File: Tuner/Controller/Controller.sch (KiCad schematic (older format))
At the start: 94 parts, among them J1 Conn_02x05_Odd_Even, J10 Conn_01x05, J12 Conn_01x02, J15 Conn_01x02, J16 Conn_01x06, J18 Conn_01x01, J19 Conn_01x01, J2 Conn_02x05_Odd_Even, J20 Conn_01x01, J21 Conn_01x01, J26 Conn_01x02, J27 Conn_01x02, J28 Conn_01x02, J3 Conn_02x05_Odd_Even, J30 Conn_01x02, J4 Conn_02x05_Odd_Even, J5 Conn_02x05_Odd_Even, J6 Conn_01x02, J7 Conn_01x02, J8 Conn_01x06, Q2 2N3904, U4 LM350_TO220

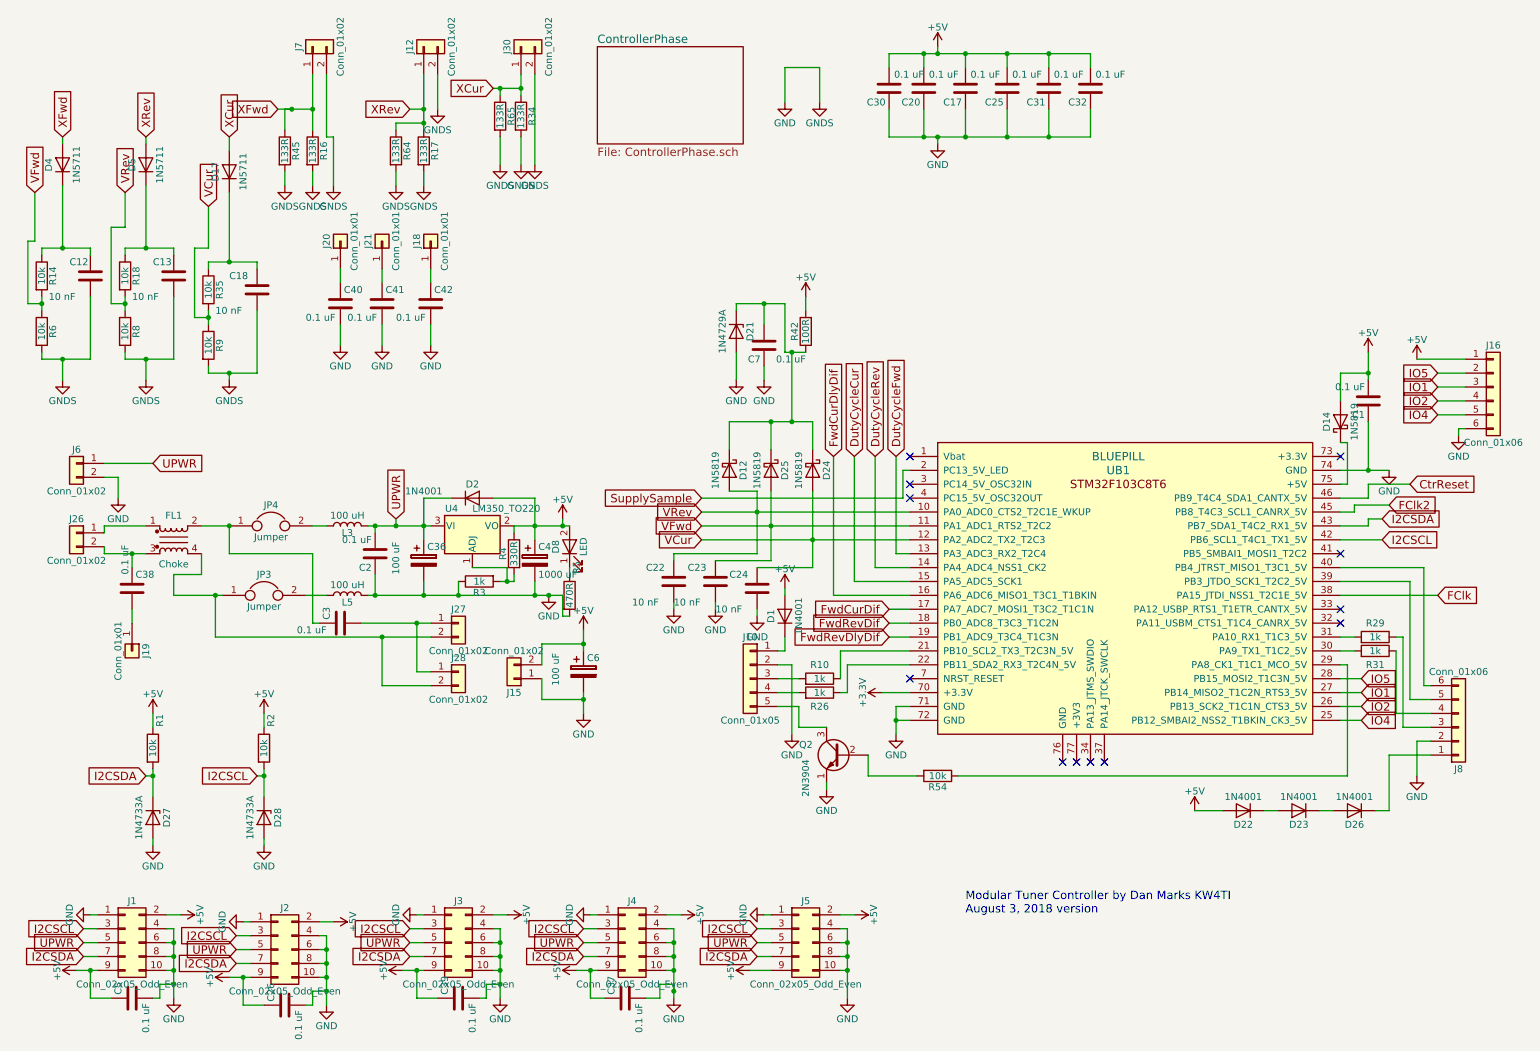
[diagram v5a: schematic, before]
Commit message: Added BNC and screw terminal combo pads
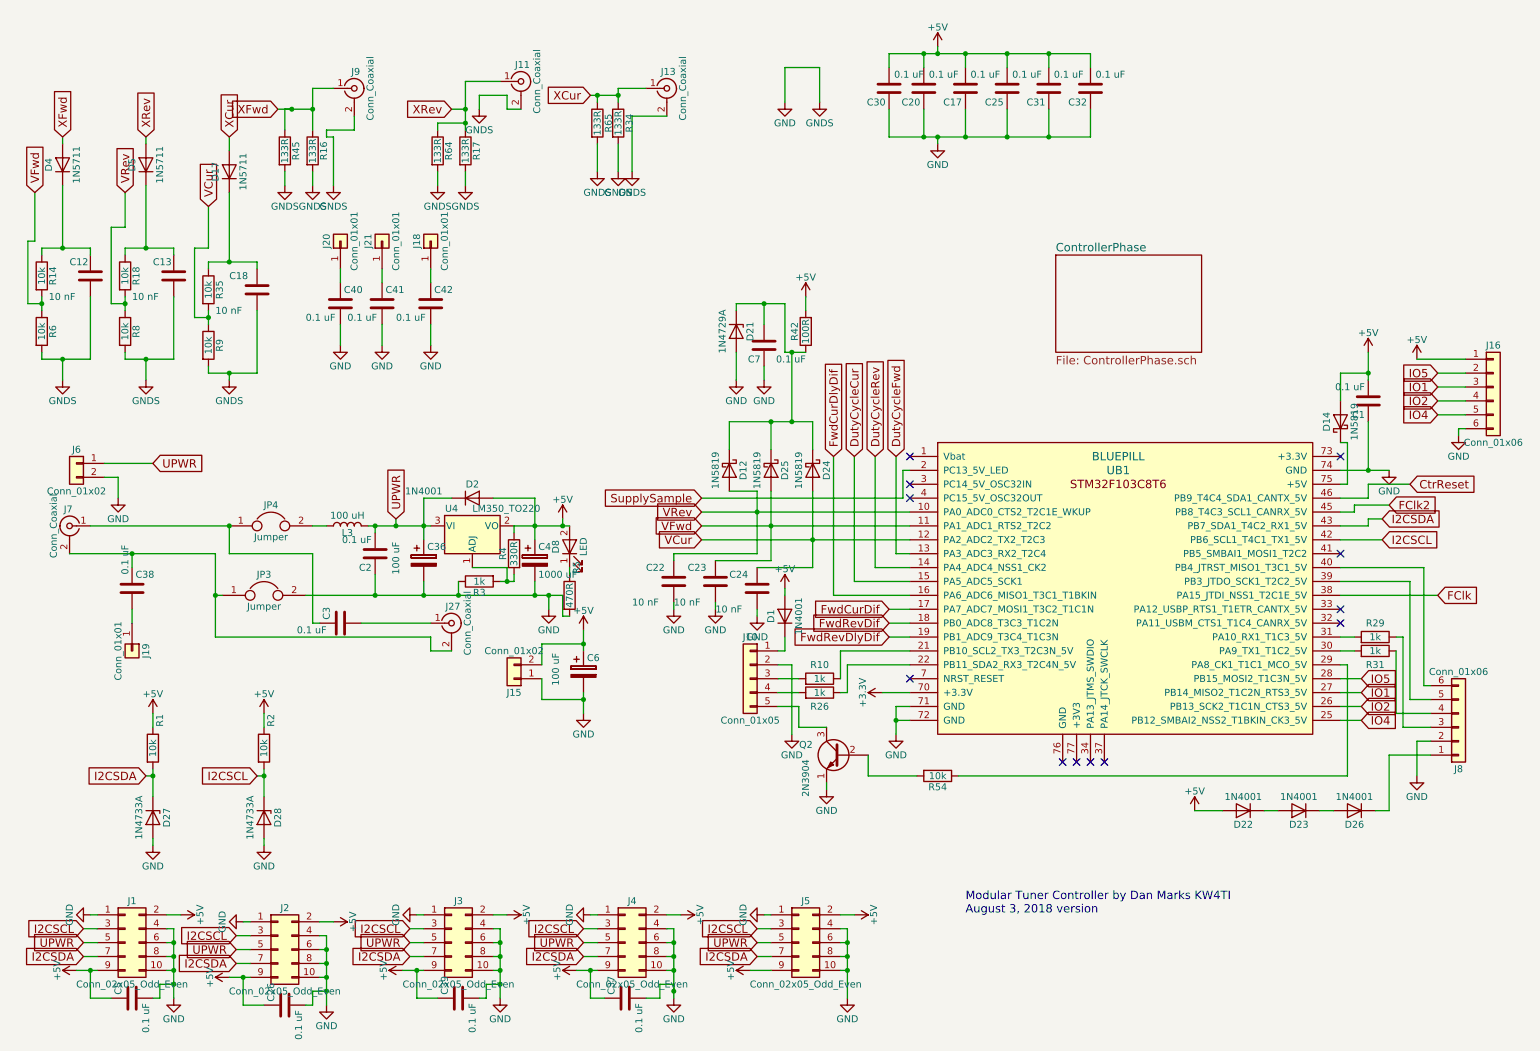
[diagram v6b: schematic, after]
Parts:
- removed FL1: Choke, Controller:GenericCMCL, symbol EMI_Filter_CommonMode
- removed J12, J26, J27, J28, J30, J7: Conn_01x02, Connectors_Terminal_Blocks:TerminalBlock_bornier-2_P5.08mm, symbol Conn_01x02
- removed L5: 100 uH, Inductors_THT:L_Toroid_Vertical_L14.0mm_W6.3mm_P4.57mm_Pulse_A, symbol L
- added J11, J13, J27, J7, J9: Conn_Coaxial, Controller:bnc_90_1-1337543-0_pad_combo, symbol Conn_Coaxial
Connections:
- net GND: now also JP3.2, J11.2 (Ext), J13.2 (Ext), J9.2 (Ext)
- net XCur: now also J13.1 (In)
- net XFwd: now also J9.1 (In)
- net XRev: now also J11.1 (In)
- net at C38.1: now also JP3.1, J27.2 (Ext), J7.2 (Ext)
- net at C3.2: now also J27.1 (In)
- net at C3.1, JP4.1: now also J7.1 (In)
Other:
- moved on the sheet: R17, R34, R64, R65

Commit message: A few tweaks
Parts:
- removed D22, D23, D26: 1N4001, Diodes_THT:D_DO-41_SOD81_P7.62mm_Horizontal, symbol D
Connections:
- net +5V: now also J8.1 (Pin_1)

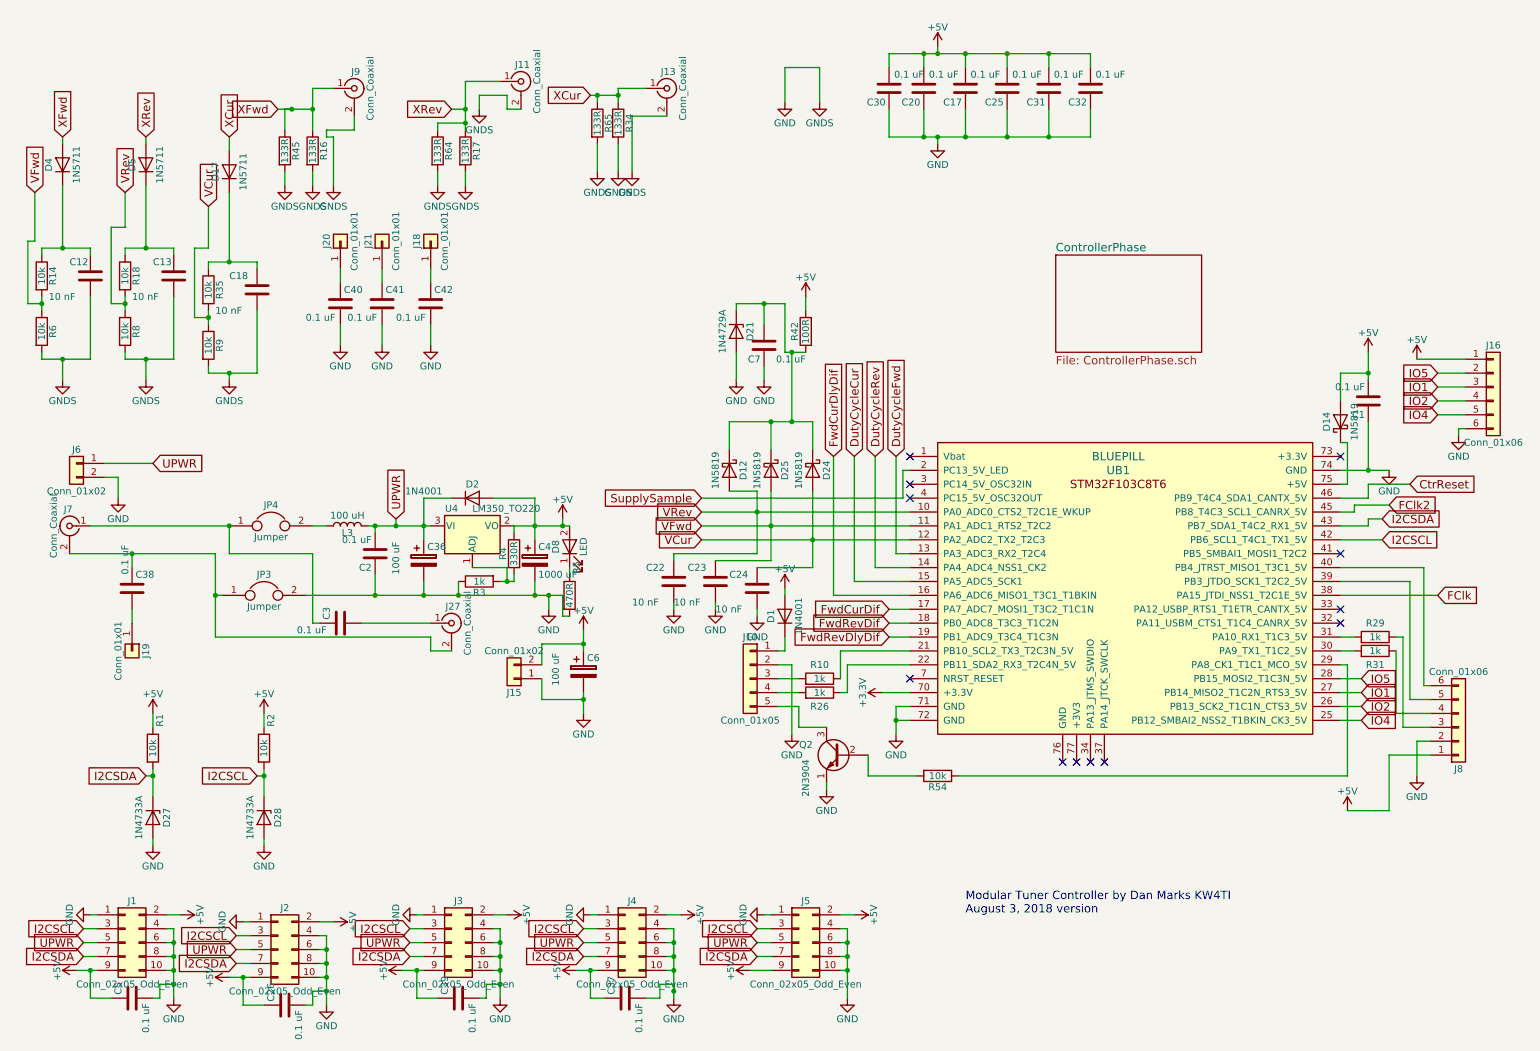
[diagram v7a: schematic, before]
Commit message: Put level shifters into controller
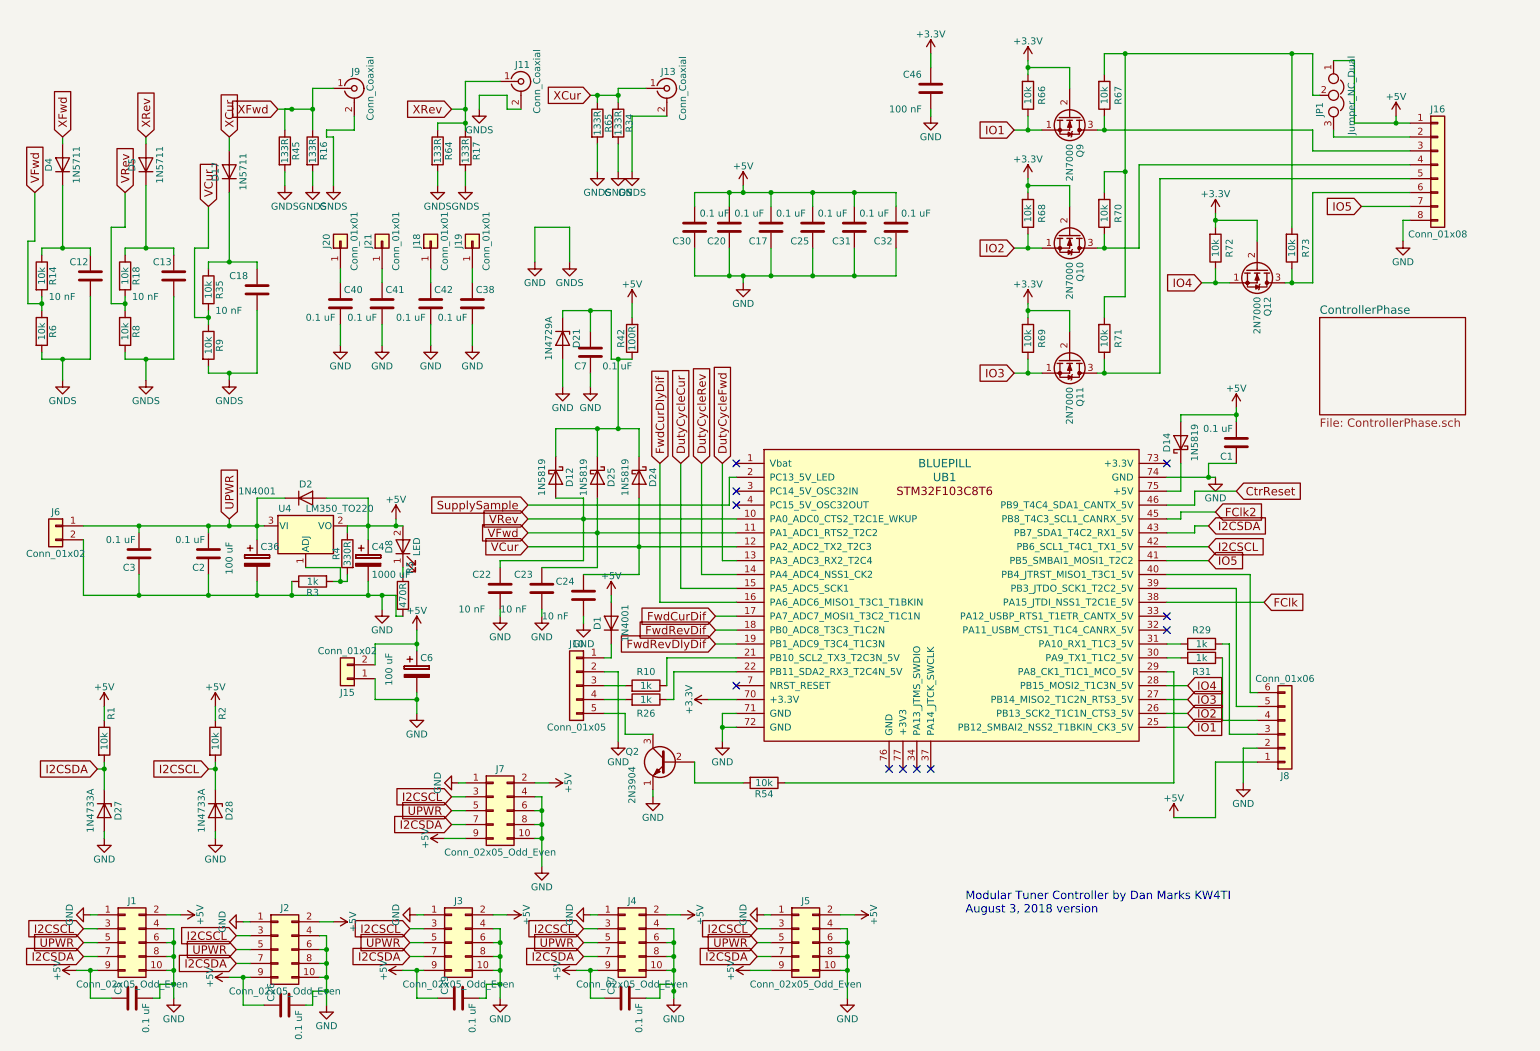
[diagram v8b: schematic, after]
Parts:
- removed J16: Conn_01x06, Pin_Headers:Pin_Header_Straight_1x06_Pitch2.54mm, symbol Conn_01x06
- removed J27, J7: Conn_Coaxial, Controller:bnc_90_1-1337543-0_pad_combo, symbol Conn_Coaxial
- removed JP3, JP4: Jumper, Pin_Headers:Pin_Header_Straight_1x02_Pitch2.54mm, symbol Jumper
- removed L3: 100 uH, Inductors_THT:L_Toroid_Vertical_L14.0mm_W6.3mm_P4.57mm_Pulse_A, symbol L
- added C46: 100 nF, Capacitors_THT:C_Disc_D5.0mm_W2.5mm_P2.50mm, symbol C
- added J16: Conn_01x08, Pin_Headers:Pin_Header_Straight_1x08_Pitch2.54mm, symbol Conn_01x08
- added J7: Conn_02x05_Odd_Even, Pin_Headers:Pin_Header_Straight_2x05_Pitch2.54mm, symbol Conn_02x05_Odd_Even
- added JP1: Jumper_NC_Dual, Pin_Headers:Pin_Header_Straight_1x03_Pitch2.54mm, symbol Jumper_NC_Dual
- added Q10, Q11, Q12, Q9: 2N7000, TO_SOT_Packages_THT:TO-92_Molded_Narrow, symbol 2N7000
- added R66, R67, R68, R69, R70, R71, R72, R73: 10k, Resistors_THT:R_Axial_DIN0207_L6.3mm_D2.5mm_P7.62mm_Horizontal, symbol R
- C3, C38: footprint Capacitors_THT:C_Disc_D10.0mm_W2.5mm_P5.00mm -> Capacitors_THT:C_Disc_D5.0mm_W2.5mm_P2.50mm
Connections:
- net +3V3: now also C46.1, Q10.2 (G), Q11.2 (G), Q12.2 (G), Q9.2 (G), R66.2, R68.2, R69.2, R72.2
- net +5V: now also J16.1 (Pin_1), J7.2 (Pin_2), J7.9 (Pin_9), JP1.1
- net GND: now also C3.1, C38.2, C46.2, J16.8 (Pin_8), J7.1 (Pin_1), J7.10 (Pin_10), J7.4 (Pin_4), J7.6 (Pin_6), J7.8 (Pin_8)
- net I2CSCL: now also J7.3 (Pin_3)
- net I2CSDA: now also J7.7 (Pin_7)
- net IO1: now also UB1.25 (PB12_SMBAI2_NSS2_T1BKIN_CK3_5V), Q9.1 (S), R66.1; no longer UB1.27 (PB14_MISO2_T1C2N_RTS3_5V)
- net IO2: now also Q10.1 (S), R68.1
- net IO4: now also UB1.28 (PB15_MOSI2_T1C3N_5V), Q12.1 (S), R72.1; no longer UB1.25 (PB12_SMBAI2_NSS2_T1BKIN_CK3_5V)
- net IO5: now also UB1.41 (PB5_SMBAI1_MOSI1_T2C2), J16.7 (Pin_7); no longer UB1.28 (PB15_MOSI2_T1C3N_5V)
- net UPWR: now also C3.2, J7.5 (Pin_5)
- net at J19.1 (Pin_1): now also C38.1; no longer C38.2
- new net: J16.2 (Pin_2), JP1.3
- new net: J16.3 (Pin_3), Q9.3 (D), R67.1
- new net: J16.4 (Pin_4), Q10.3 (D), R70.1
- new net: J16.5 (Pin_5), Q11.3 (D), R71.1
- new net: J16.6 (Pin_6), Q12.3 (D), R73.1
- new net: JP1.2, R67.2, R70.2, R71.2, R73.2
- new net IO3: Q11.1 (S), R69.1, UB1.27 (PB14_MISO2_T1C2N_RTS3_5V)
- no-connect marks 12 -> 11
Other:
- moved on the sheet: C1, C17, C2, C20, C22, C23, C24, C25, C30, C31, C32, C36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
